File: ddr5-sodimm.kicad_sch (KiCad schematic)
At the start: 19 parts, among them J4001 BUS_DDR5_SODIMM_AMPHENOL_1016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

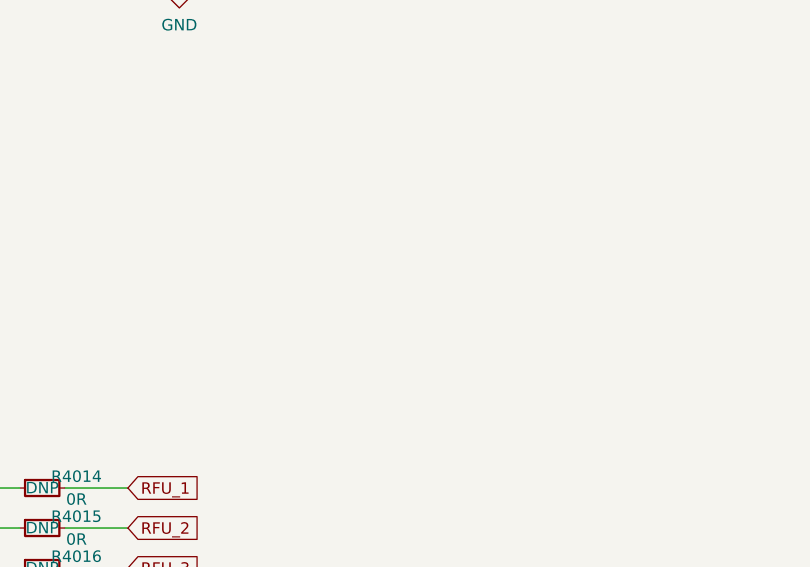
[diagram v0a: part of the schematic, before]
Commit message: Improve PCB after layout review
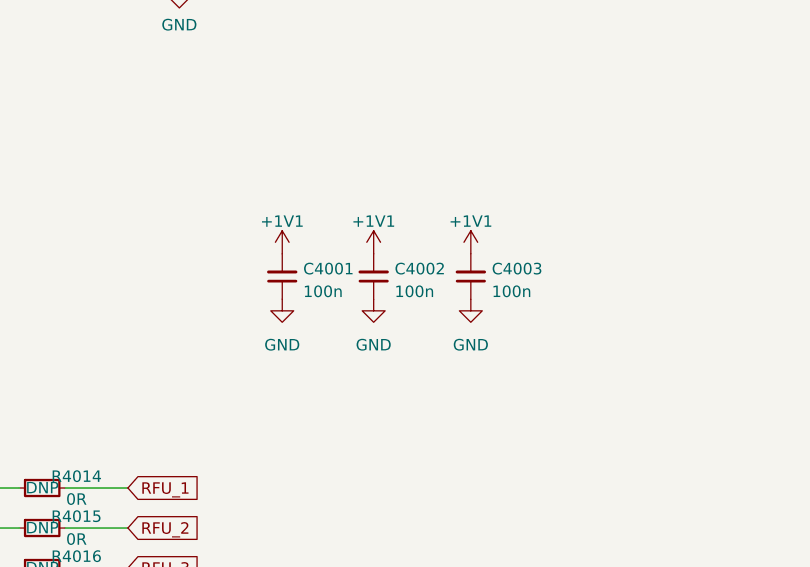
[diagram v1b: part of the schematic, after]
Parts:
- added C4001, C4002, C4003: C_100n_0402, antmicro-footprints:C_0402_1005Metric, symbol antmicroCapacitors0402:C_100n_0402
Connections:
- net +1V1: now also C4001.2, C4002.2, C4003.2
- net GND: now also C4001.1, C4002.1, C4003.1

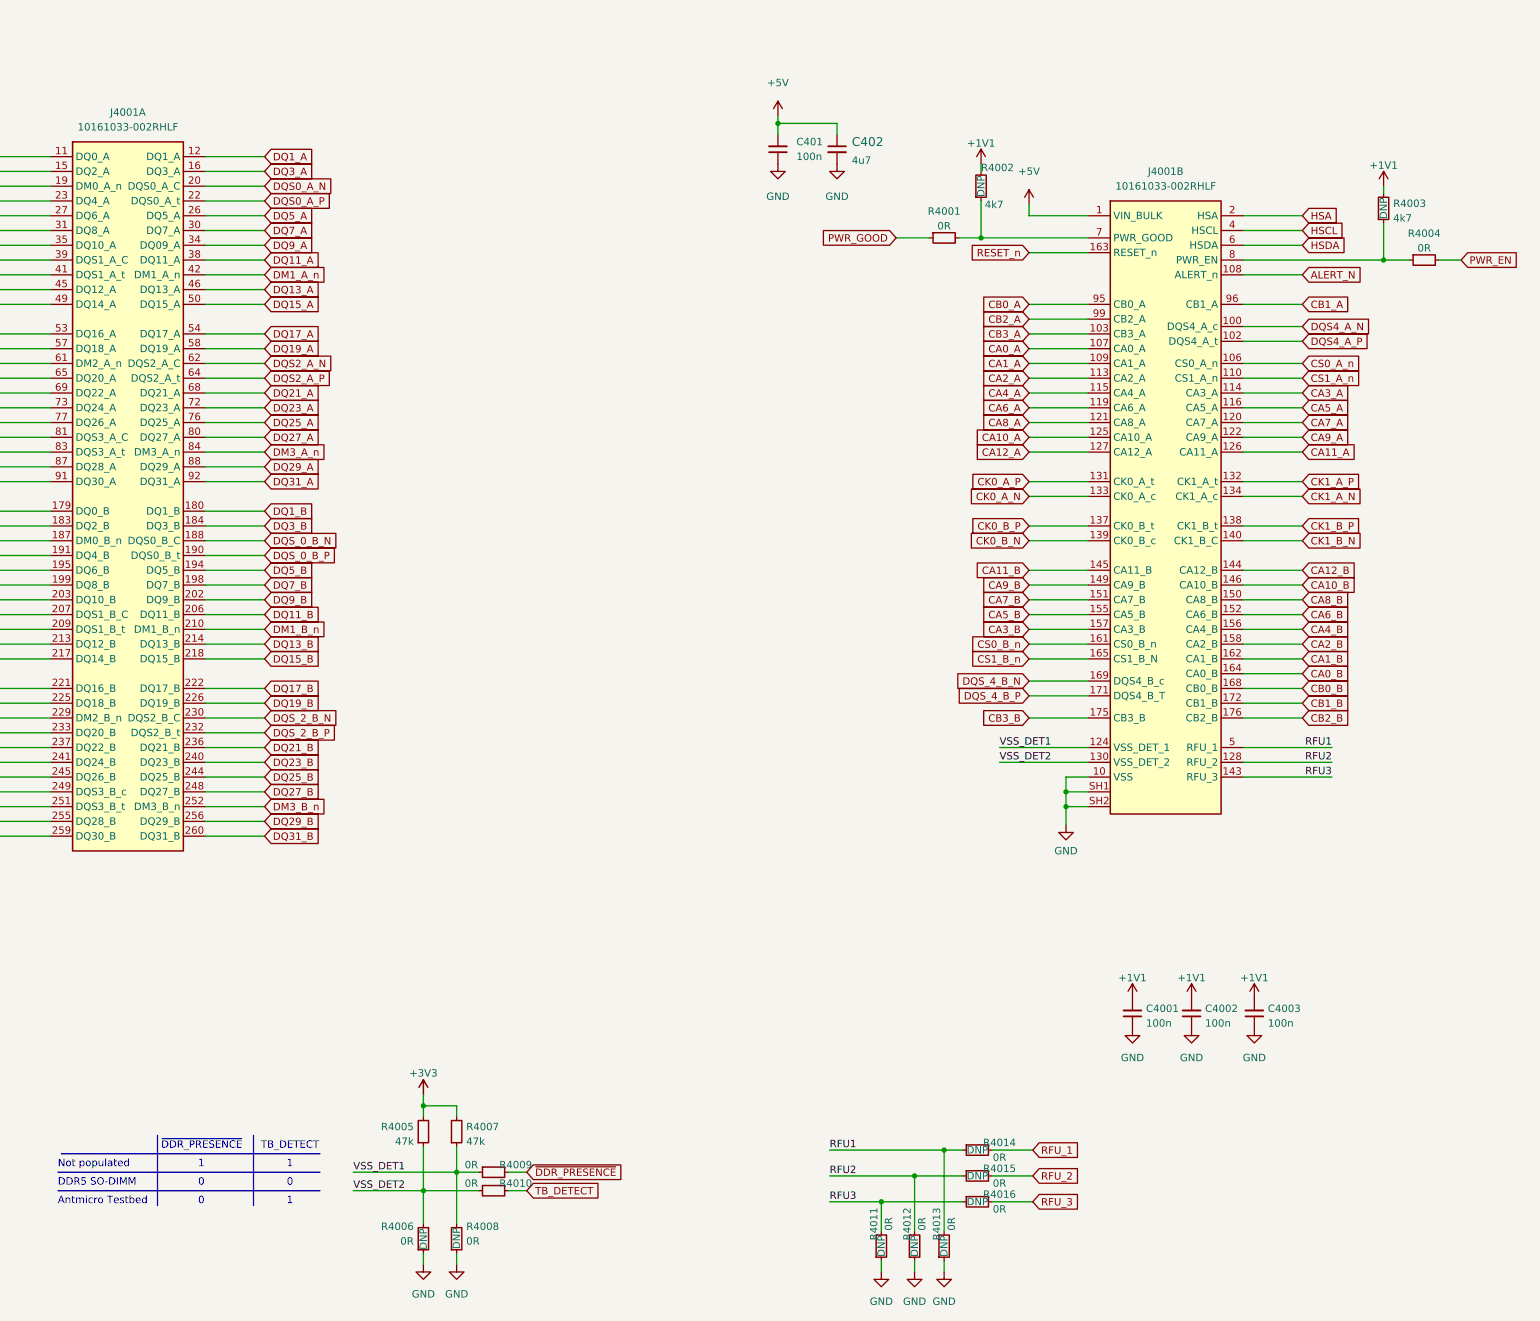
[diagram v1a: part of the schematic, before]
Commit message: Re-annotate schematic
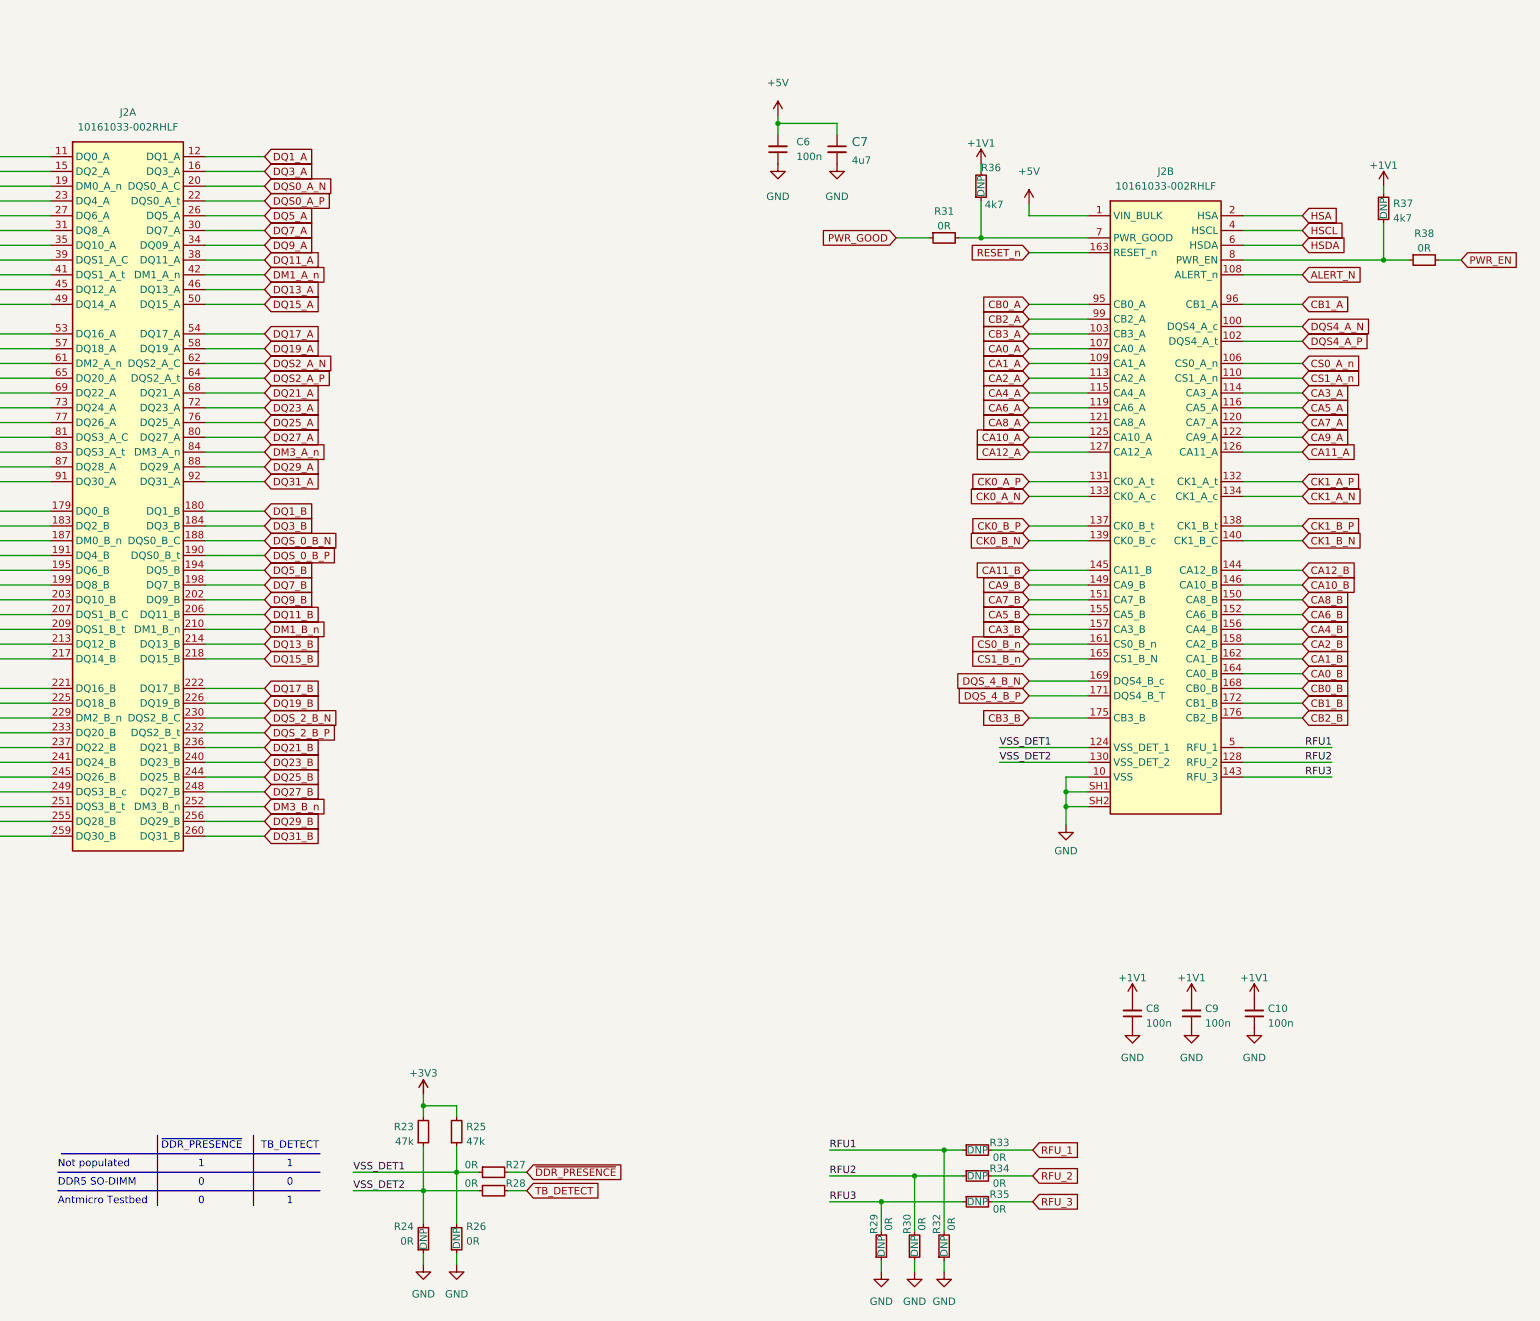
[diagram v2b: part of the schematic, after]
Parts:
- renumbered C4003 to C10, C401 to C6, C402 to C7, C4001 to C8, C4002 to C9, J4001 to J2, R4005 to R23, R4006 to R24, R4007 to R25, R4008 to R26, R4009 to R27, R4010 to R28, R4011 to R29, R4012 to R30, R4001 to R31, R4013 to R32, R4014 to R33, R4015 to R34, R4016 to R35, R4002 to R36, R4003 to R37, R4004 to R38

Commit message: Add local libraries
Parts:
- C10, C8, C9: footprint antmicro-footprints:C_0402_1005Metric -> sodimm-ddr5-tester-footprints:C_0402_1005Metric; symbol antmicroCapacitors0402:C_100n_0402 -> sodimm-ddr5-tester:C_100n_0402
- J2: footprint antmicro-footprints:DDR5_AMPHENOL_10161033-002RHLF -> sodimm-ddr5-tester-footprints:DDR5_AMPHENOL_10161033-002RHLF; symbol antmicroMemoryConnectorsPCCardSockets:BUS_DDR5_SODIMM_AMPHENOL_10161033-002RHLF -> sodimm-ddr5-tester:BUS_DDR5_SODIMM_AMPHENOL_10161033-002RHLF
- R23, R25: footprint antmicro-footprints:R_0402_1005Metric -> sodimm-ddr5-tester-footprints:R_0402_1005Metric; symbol antmicroResistors0402:R_47k_0402 -> sodimm-ddr5-tester:R_47k_0402
- R24, R26, R27, R28, R29, R30, R31, R32, R33, R34, R35, R38: footprint antmicro-footprints:R_0402_1005Metric -> sodimm-ddr5-tester-footprints:R_0402_1005Metric; symbol antmicroResistors0402:R_0R_0402 -> sodimm-ddr5-tester:R_0R_0402
- R36, R37: footprint antmicro-footprints:R_0402_1005Metric -> sodimm-ddr5-tester-footprints:R_0402_1005Metric; symbol antmicroResistors0402:R_4k7_0402 -> sodimm-ddr5-tester:R_4k7_0402

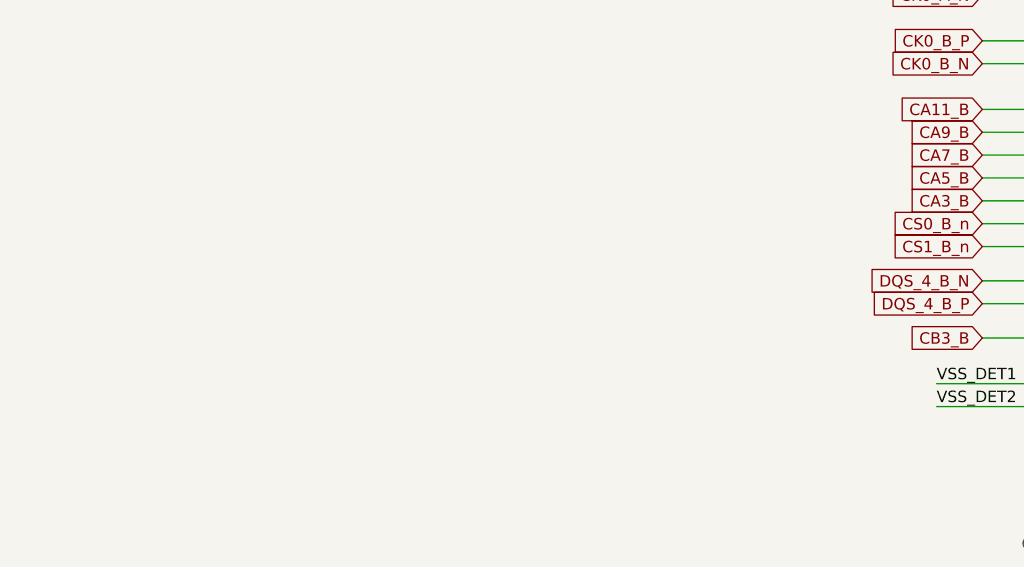
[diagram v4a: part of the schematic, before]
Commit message: Define DDR5, HyperBus and I2C buses. Connect HyperRAM with hierarchical bus
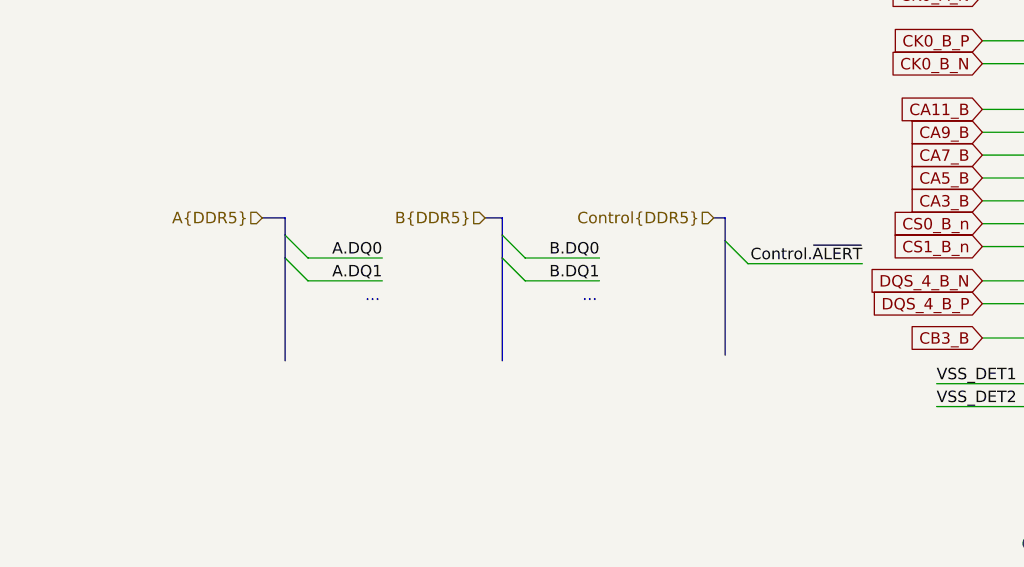
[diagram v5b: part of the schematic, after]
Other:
- note added: "..."
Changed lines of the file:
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@@
   (junction (at 253.365 252.095) (diameter 0) (color 0 0 0 0)
   )
+  (bus_entry (at 239.395 167.005) (size 2.54 2.54)
+    (stroke (width 0) (type default) (color 0 0 0 0))
+  )
+  (bus_entry (at 214.63 168.91) (size 2.54 2.54)
+    (stroke (width 0) (type default) (color 0 0 0 0))
+  )
+  (bus_entry (at 190.5 168.91) (size 2.54 2.54)
+    (stroke (width 0) (type default) (color 0 0 0 0))
+  )
+  (bus_entry (at 214.63 166.37) (size 2.54 2.54)
+    (stroke (width 0) (type default) (color 0 0 0 0))
+  )
+  (bus_entry (at 190.5 166.37) (size 2.54 2.54)
+    (stroke (width 0) (type default) (color 0 0 0 0))
+  )
   (polyline (pts (xy 118.11 249.555) (xy 118.11 261.62))
     (stroke (width 0) (type default) (color 0 0 0 0))
@@
     (stroke (width 0) (type default) (color 0 0 0 0))
   )
+  (bus (pts (xy 212.725 164.465) (xy 214.63 164.465))
+    (stroke (width 0) (type default) (color 0 0 0 0))
+  )
   (wire (pts (xy 267.97 97.79) (xy 278.13 97.79))
     (stroke (width 0) (type default) (color 0 0 0 0))
@@
     (stroke (width 0) (type default) (color 0 0 0 0))
   )
+  (wire (pts (xy 241.935 169.545) (xy 254.635 169.545))
+    (stroke (width 0) (type default) (color 0 0 0 0))
+  )
   (wire (pts (xy 89.535 198.12) (xy 99.695 198.12))
     (stroke (width 0) (type default) (color 0 0 0 0))
   )
+  (bus (pts (xy 239.395 167.005) (xy 239.395 179.705))
+    (stroke (width 0) (type default) (color 0 0 0 0))
+  )
   (wire (pts (xy 267.97 177.8) (xy 278.13 177.8))
     (stroke (width 0) (type default) (color 0 0 0 0))
@@
     (stroke (width 0) (type default) (color 0 0 0 0))
   )
+  (wire (pts (xy 193.04 171.45) (xy 201.295 171.45))
+    (stroke (width 0) (type default) (color 0 0 0 0))
+  )
   (wire (pts (xy 126.365 101.6) (xy 136.525 101.6))
     (stroke (width 0) (type default) (color 0 0 0 0))
@@
     (stroke (width 0) (type default) (color 0 0 0 0))
   )
+  (bus (pts (xy 190.5 164.465) (xy 190.5 166.37))
+    (stroke (width 0) (type default) (color 0 0 0 0))
+  )
   (wire (pts (xy 89.535 144.78) (xy 99.695 144.78))
     (stroke (width 0) (type default) (color 0 0 0 0))
@@
     (stroke (width 0) (type default) (color 0 0 0 0))
   )
+  (bus (pts (xy 190.5 168.91) (xy 190.5 180.34))
+    (stroke (width 0) (type default) (color 0 0 0 0))
+  )
   (wire (pts (xy 126.365 162.56) (xy 136.525 162.56))
     (stroke (width 0) (type default) (color 0 0 0 0))
@@
     (stroke (width 0) (type default) (color 0 0 0 0))
   )
+  (wire (pts (xy 217.17 168.91) (xy 225.425 168.91))
+    (stroke (width 0) (type default) (color 0 0 0 0))
+  )
   (wire (pts (xy 304.8 160.02) (xy 314.96 160.02))
     (stroke (width 0) (type default) (color 0 0 0 0))
@@
     (stroke (width 0) (type default) (color 0 0 0 0))
   )
+  (bus (pts (xy 238.125 164.465) (xy 239.395 164.465))
+    (stroke (width 0) (type default) (color 0 0 0 0))
+  )
   (wire (pts (xy 314.96 177.8) (xy 304.8 177.8))
     (stroke (width 0) (type default) (color 0 0 0 0))
@@
     (stroke (width 0) (type default) (color 0 0 0 0))
   )
+  (bus (pts (xy 214.63 166.37) (xy 214.63 168.91))
+    (stroke (width 0) (type default) (color 0 0 0 0))
+  )
   (wire (pts (xy 314.96 93.98) (xy 304.8 93.98))
     (stroke (width 0) (type default) (color 0 0 0 0))
@@
     (stroke (width 0) (type default) (color 0 0 0 0))
   )
+  (bus (pts (xy 187.96 164.465) (xy 190.5 164.465))
+    (stroke (width 0) (type default) (color 0 0 0 0))
+  )
   (wire (pts (xy 89.535 182.88) (xy 99.695 182.88))
     (stroke (width 0) (type default) (color 0 0 0 0))
@@
     (stroke (width 0) (type default) (color 0 0 0 0))
   )
+  (bus (pts (xy 214.63 168.91) (xy 214.63 180.34))
+    (stroke (width 0) (type default) (color 0 0 0 0))
+  )
   (wire (pts (xy 89.535 185.42) (xy 99.695 185.42))
     (stroke (width 0) (type default) (color 0 0 0 0))
@@
     (stroke (width 0) (type default) (color 0 0 0 0))
   )
+  (wire (pts (xy 217.17 171.45) (xy 225.425 171.45))
+    (stroke (width 0) (type default) (color 0 0 0 0))
+  )
   (wire (pts (xy 261.62 256.54) (xy 268.605 256.54))
     (stroke (width 0) (type default) (color 0 0 0 0))
@@
     (stroke (width 0) (type default) (color 0 0 0 0))
   )
+  (wire (pts (xy 193.04 168.91) (xy 201.295 168.91))
+    (stroke (width 0) (type default) (color 0 0 0 0))
+  )
   (wire (pts (xy 328.93 99.06) (xy 304.8 99.06))
     (stroke (width 0) (type default) (color 0 0 0 0))
@@
     (stroke (width 0) (type default) (color 0 0 0 0))
   )
+  (bus (pts (xy 239.395 164.465) (xy 239.395 167.005))
+    (stroke (width 0) (type default) (color 0 0 0 0))
+  )
   (wire (pts (xy 245.11 95.25) (xy 250.825 95.25))
     (stroke (width 0) (type default) (color 0 0 0 0))
@@
     (stroke (width 0) (type default) (color 0 0 0 0))
   )
+  (bus (pts (xy 190.5 166.37) (xy 190.5 168.91))
+    (stroke (width 0) (type default) (color 0 0 0 0))
+  )
   (wire (pts (xy 126.365 88.9) (xy 136.525 88.9))
     (stroke (width 0) (type default) (color 0 0 0 0))
@@
     (stroke (width 0) (type default) (color 0 0 0 0))
   )
+  (bus (pts (xy 214.63 164.465) (xy 214.63 166.37))
+    (stroke (width 0) (type default) (color 0 0 0 0))
+  )
   (wire (pts (xy 314.96 121.92) (xy 304.8 121.92))
     (stroke (width 0) (type default) (color 0 0 0 0))
@@
     (effects (font (size 1.27 1.27)) (justify left bottom))
   )
+  (text "..." (at 199.39 173.99 0)
+    (effects (font (size 1.27 1.27)) (justify left bottom))
+  )
   (text "~{DDR_PRESENCE}" (at 118.745 252.095 0)
     (effects (font (size 1.27 1.27)) (justify left bottom))
@@
     (effects (font (size 1.27 1.27)) (justify left bottom))
   )
+  (text "..." (at 223.52 173.99 0)
+    (effects (font (size 1.27 1.27)) (justify left bottom))
+  )
   (text "1" (at 125.095 255.27 0)
     (effects (font (size 1.27 1.27)) (justify left bottom))
   )
+  (label "A.DQ0" (at 201.295 168.91 180)
+    (effects (font (size 1.27 1.27)) (justify right bottom))
+  )
   (label "VSS_DET1" (at 151.765 255.905 0)
     (effects (font (size 1.27 1.27)) (justify left bottom))
@@
     (effects (font (size 1.27 1.27)) (justify right bottom))
   )
+  (label "B.DQ0" (at 225.425 168.91 180)
+    (effects (font (size 1.27 1.27)) (justify right bottom))
+  )
   (label "RFU3" (at 233.68 260.985 0)
     (effects (font (size 1.27 1.27)) (justify left bottom))
   )
+  (label "A.DQ1" (at 201.295 171.45 180)
+    (effects (font (size 1.27 1.27)) (justify right bottom))
+  )
+  (label "B.DQ1" (at 225.425 171.45 180)
+    (effects (font (size 1.27 1.27)) (justify right bottom))
+  )
   (label "RFU2" (at 320.04 185.42 180)
     (effects (font (size 1.27 1.27)) (justify right bottom))
@@
     (effects (font (size 1.27 1.27)) (justify left bottom))
   )
+  (label "Control.~{ALERT}" (at 254.635 169.545 180)
+    (effects (font (size 1.27 1.27)) (justify right bottom))
+  )
   (global_label "CA12_A" (shape input) (at 267.97 132.08 180) (fields_autoplaced)
     (effects (font (size 1.27 1.27)) (justify right))
@@
     )
   )
+  (hierarchical_label "Control{DDR5}" (shape input) (at 238.125 164.465 180)
+    (effects (font (size 1.27 1.27)) (justify right))
+  )
+  (hierarchical_label "B{DDR5}" (shape input) (at 212.725 164.465 180)
+    (effects (font (size 1.27 1.27)) (justify right))
+  )
+  (hierarchical_label "A{DDR5}" (shape input) (at 187.96 164.465 180)
+    (effects (font (size 1.27 1.27)) (justify right))
+  )
   (symbol (lib_id "sodimm-ddr5-tester:GND") (at 306.705 231.14 0) (unit 1)
